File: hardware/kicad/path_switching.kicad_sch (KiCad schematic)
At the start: 25 parts, among them J601 VIN, Q601 CSD17577Q3A, Q602 CSD17577Q3A, Q603 CSD17577Q3A, Q604 CSD17577Q3A, U601 TC4427EOA, U602 MCP6561T-E/OT

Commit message: feat(hardware)!: draw draft A1 of the schematic around a Pico 2
A Raspberry Pi Pico 2 on two 1x20 sockets replaces the ESP32-S3
development board, the programmable logic device and the buffer
between the two boards (D-39 to D-43 of the specification). The former
interface and range logic sheets become two new ones:

- Controller: the Pico 2, the diodes that join its USB supply and the
  5 V rail of the carrier, resistor arrays in the SPI and acquisition
  lines, a reset button and a console header.
- Side Data: two shift registers that take the range, the status
  signals and the eight logic inputs with every sample.

The DUT connects through a 1x4 pin header and a lever terminal block
in parallel, both GND, VIN, VOUT, GND, and the logic port is a 1x10
header with VCC, GND, D7 to D0: the pin order of the PPK2 (D-44). A
solder jumper selects the supply of the DUT side of the level
translator. A transistor at the driver of the ampere switch holds it
open while VIN is above 5.5 V.

Reference designators are numbered as the annotation tool of KiCad
does by default (D-45). The numbering touches every sheet, so these
changes come in one commit. The symbol and the socket footprint of
the ESP32-S3 board leave the project library; the Pico 2 uses the
symbol and the footprint of the KiCad library.

The electrical rules check reports no errors and no warnings. The
parts stay candidates, and no program for the PIO blocks exists yet.

BREAKING CHANGE: the pins of the controller follow the new pin map of
section 5 of the specification.
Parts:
- removed J601: VIN, TerminalBlock_Phoenix:TerminalBlock_Phoenix_MKDS-1,5-2-5.08_1x02_P5.08mm_Horizontal, symbol Connector:Screw_Terminal_01x02
- added Q1: BSS138, Package_TO_SOT_SMD:SOT-23, symbol Transistor_FET:BSS138
- added R28: 1k, Resistor_SMD:R_0603_1608Metric, symbol Device:R
- R29: renamed from R606; value 1k -> 10k
- renumbered C601 to C41, C602 to C42, C603 to C43, C604 to C44, C605 to C45, D601 to D6, F601 to F2, Q601 to Q2, Q603 to Q3, Q602 to Q4, Q604 to Q5, R605 to R27, R607 to R30, R608 to R31, R609 to R32, R602 to R33, R601 to R34, R603 to R35, R604 to R36, TP602 to TP14, TP601 to TP15, U601 to U13, U602 to U14
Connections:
- net GATE_AMP: now also R28.1; no longer R29.1, U13.4 (IN_B)
- net GND: now also Q1.2 (S)
- net VIN_OV: now also Q1.1 (G)
- net VIN_RAW: now reaches F2.1
- new net: Q1.3 (D), R28.2, R29.1, U13.4 (IN_B)
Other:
- note added: "Mode switches: back-to-back pairs, gates at +12 V_A. Both off at reset; the controller breaks one before it makes the other. VIN: F2 and D6 take a reversed supply. VIN_OV goes high above 5.5 V and Q1 then holds the ampere switch open (it blocks up to 30 V), whatever the controller asks."
- note removed: "Mode switches: back-to-back pairs, gates at +12 V_A. Both off at reset; the logic device breaks one before it makes the other. VIN: F601 and D601 take a reversed supply. VIN_OV goes high above 5.5 V and the logic device then keeps the ampere switch open (blocks up to 30 V)."
- moved on the sheet: R27

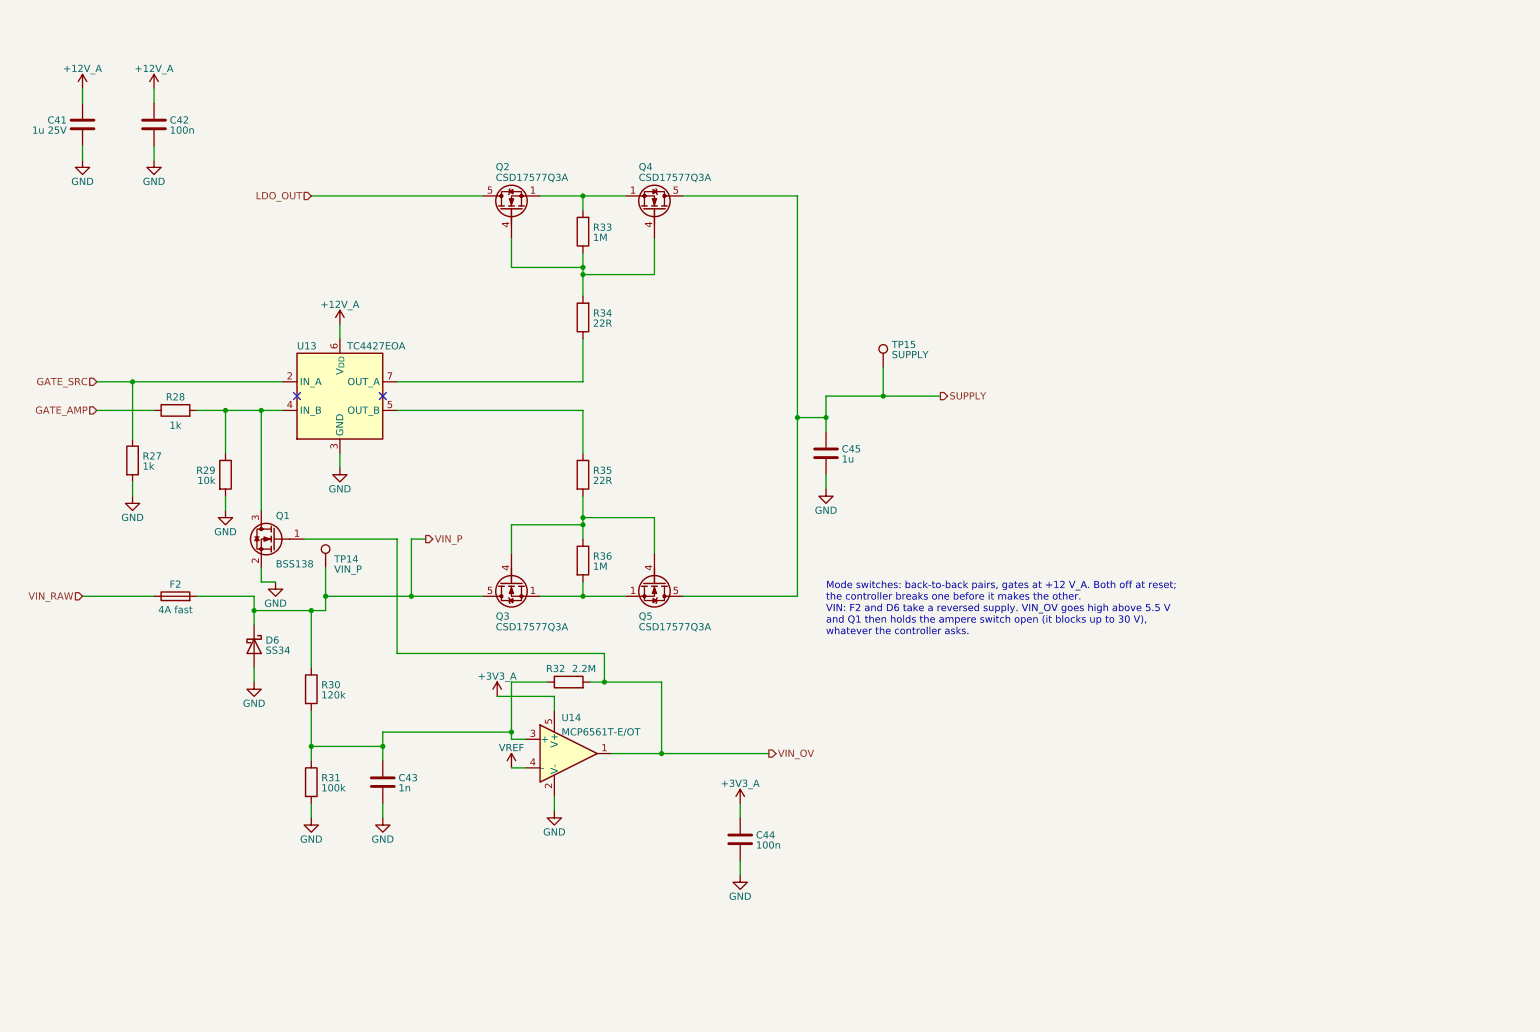
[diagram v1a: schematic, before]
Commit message: feat(hardware): draw draft A2 of the schematic
428 parts on 15 A4 pages, 14 sheets below the root sheet (D-83). Two
sheets are new: Logic Supplies, with the supervisor of the 5 V rail and
the two 3.3 V regulators, and Rail Monitor, with the comparators behind
PWR_GOOD.

The drawings follow the specification of draft A2: a current limiter
on each supply input and a priority multiplexer, a pre-regulator that
tracks the output of the linear regulator, a VIN path that withstands
-20 V to +20 V with its switch open, two diode-connected MOSFETs as
ladder clamp, thin-film and four-terminal shunts, ESD arrays at the CC
pins and at the VCC pin of the logic port. The reference designators
are numbered as KiCad numbers them (D-45), so they are not those of
draft A1.

The project library gains the symbol of the input multiplexer and two
footprints: the lever terminal block with pads of 1.9 mm x 2.3 mm and
the controller module without its antenna keep-out (D-85).

The electrical rules check reports no errors and no warnings. The
parts are candidates, and nothing is built or measured.
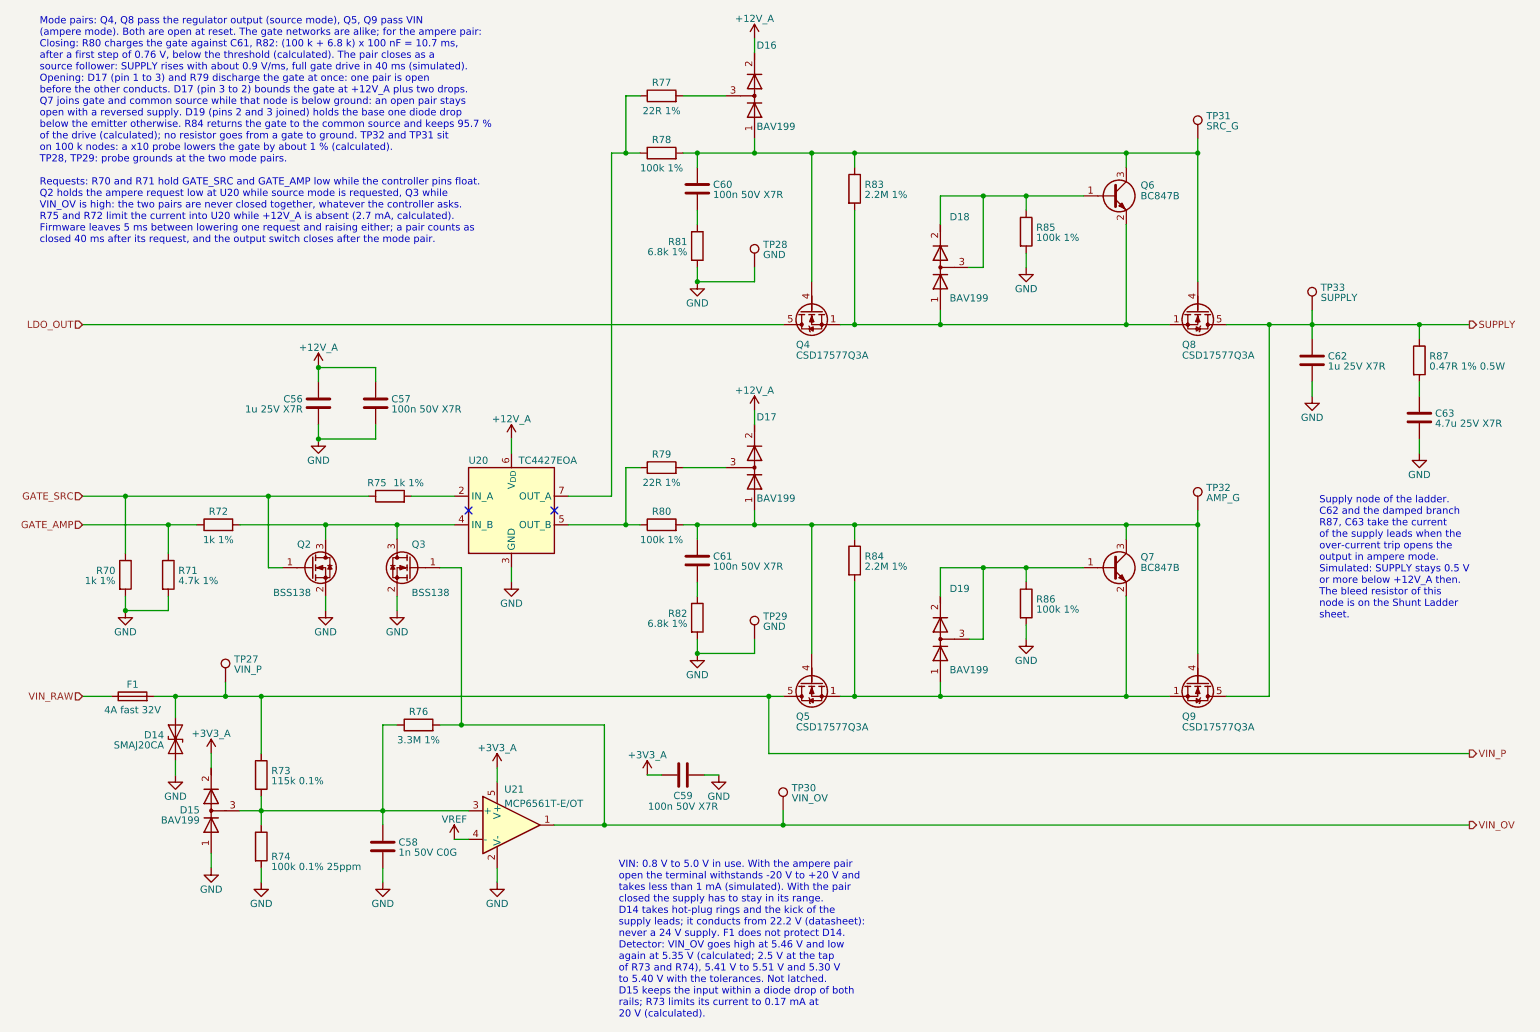
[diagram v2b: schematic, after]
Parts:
- added C60, C61: 100n 50V X7R, Capacitor_SMD:C_0603_1608Metric, symbol Device:C
- added C63: 4.7u 25V X7R, Capacitor_SMD:C_0805_2012Metric, symbol Device:C
- added D15, D16, D17, D18, D19: BAV199, Package_TO_SOT_SMD:SOT-23, symbol Device:D_Dual_Series_AKC
- added Q2: BSS138, Package_TO_SOT_SMD:SOT-23, symbol Transistor_FET:BSS138
- added Q6, Q7: BC847B, Package_TO_SOT_SMD:SOT-23, symbol Transistor_BJT:BC847
- added R75: 1k 1%, Resistor_SMD:R_0603_1608Metric, symbol Device:R
- added R78, R80, R85, R86: 100k 1%, Resistor_SMD:R_0603_1608Metric, symbol Device:R
- added R81, R82: 6.8k 1%, Resistor_SMD:R_0603_1608Metric, symbol Device:R
- added R87: 0.47R 1% 0.5W, Resistor_SMD:R_1206_3216Metric, symbol Device:R
- added TP28, TP29: GND, TestPoint:TestPoint_Pad_2.0x2.0mm, symbol Connector:TestPoint
- added TP30: VIN_OV, TestPoint:TestPoint_Pad_D1.5mm, symbol Connector:TestPoint
- added TP31: SRC_G, TestPoint:TestPoint_Pad_D1.5mm, symbol Connector:TestPoint
- added TP32: AMP_G, TestPoint:TestPoint_Pad_D1.5mm, symbol Connector:TestPoint
- C56: renamed from C41; value 1u 25V -> 1u 25V X7R; MPN (none) -> C0603C105K3RACTU; Manufacturer (none) -> KEMET
- C57: renamed from C42; value 100n -> 100n 50V X7R; MPN (none) -> C0603C104K5RACTU; Manufacturer (none) -> KEMET
- C58: renamed from C43; value 1n -> 1n 50V C0G; MPN (none) -> C0603C102J5GACTU; Manufacturer (none) -> KEMET
- C59: renamed from C44; value 100n -> 100n 50V X7R; MPN (none) -> C0603C104K5RACTU; Manufacturer (none) -> KEMET
- C62: renamed from C45; value 1u -> 1u 25V X7R; MPN (none) -> C0603C105K3RACTU; Manufacturer (none) -> KEMET
- D14: renamed from D6; value SS34 -> SMAJ20CA; symbol Device:D_Schottky -> Diode:SMAJ20CA; MPN (none) -> SMAJ20CA-E3/61; Manufacturer (none) -> Vishay
- F1: renamed from F2; value 4A fast -> 4A fast 32V; MPN (none) -> 0466004.NR; Manufacturer (none) -> Littelfuse
- Q3: renamed from Q1; MPN (none) -> BSS138-7-F; Manufacturer (none) -> Diodes Incorporated
- Q4: renamed from Q2; MPN (none) -> CSD17577Q3A; Manufacturer (none) -> Texas Instruments
- Q5: renamed from Q3; MPN (none) -> CSD17577Q3A; Manufacturer (none) -> Texas Instruments
- Q8: renamed from Q4; MPN (none) -> CSD17577Q3A; Manufacturer (none) -> Texas Instruments
- Q9: renamed from Q5; MPN (none) -> CSD17577Q3A; Manufacturer (none) -> Texas Instruments
- R70: renamed from R27; value 1k -> 1k 1%; MPN (none) -> CRCW06031K00FKEA; Manufacturer (none) -> Vishay
- R71: renamed from R29; value 10k -> 4.7k 1%; MPN (none) -> CRCW06034K70FKEA; Manufacturer (none) -> Vishay
- R72: renamed from R28; value 1k -> 1k 1%; MPN (none) -> CRCW06031K00FKEA; Manufacturer (none) -> Vishay
- R73: renamed from R30; value 120k -> 115k 0.1%; MPN (none) -> TNPW0603115KBEEA; Manufacturer (none) -> Vishay
- R74: renamed from R31; value 100k -> 100k 0.1% 25ppm; MPN (none) -> TNPW0603100KBEEA; Manufacturer (none) -> Vishay
- R76: renamed from R32; value 2.2M -> 3.3M 1%; MPN (none) -> CRCW06033M30FKEA; Manufacturer (none) -> Vishay
- R77: renamed from R34; value 22R -> 22R 1%; MPN (none) -> CRCW060322R0FKEA; Manufacturer (none) -> Vishay
- R79: renamed from R35; value 22R -> 22R 1%; MPN (none) -> CRCW060322R0FKEA; Manufacturer (none) -> Vishay
- R83: renamed from R33; value 1M -> 2.2M 1%; MPN (none) -> CRCW06032M20FKEA; Manufacturer (none) -> Vishay
- R84: renamed from R36; value 1M -> 2.2M 1%; MPN (none) -> CRCW06032M20FKEA; Manufacturer (none) -> Vishay
- TP27: renamed from TP14; now left out of the parts list
- TP33: renamed from TP15; now left out of the parts list
- U20: renamed from U13; MPN (none) -> TC4427EOA713; Manufacturer (none) -> Microchip
- U21: renamed from U14; MPN (none) -> MCP6561T-E/OT; Manufacturer (none) -> Microchip
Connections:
- net +12V_A: now also D16.2 (K), D17.2 (K)
- net +3V3_A: now also D15.2 (K)
- net GATE_AMP: now also R71.1
- net GATE_SRC: now also Q2.1 (G), R75.1; no longer U20.2 (IN_A)
- net GND: now also C63.2, D15.1 (A), Q2.2 (S), R81.2, R82.2, R85.2, R86.2, TP28.1, TP29.1
- net SUPPLY: now also R87.1
- net VIN_OV: now also TP30.1
- net at C58.1, R73.2, R74.1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: now also D15.3 (common)
- net at Q4.1 (S), Q4.2 (S), Q4.3 (S)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: now also D18.1 (A), Q6.2 (E)
- net at Q4.4 (G), Q8.4 (G), R83.1: now also C60.1, D16.1 (A), Q6.3 (C), R78.2, TP31.1; no longer R77.2
- net at Q3.3 (D), R72.2, U20.4 (IN_B): now also Q2.3 (D); no longer R71.1
- net at R79.1, U20.5 (OUT_B): now also R80.1
- net at Q5.4 (G), Q9.4 (G), R84.1: now also C61.1, D17.1 (A), Q7.3 (C), R80.2, TP32.1; no longer R79.2
- net at Q5.1 (S), Q5.2 (S), Q5.3 (S)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: now also D19.1 (A), Q7.2 (E)
- net at R77.1, U20.7 (OUT_A): now also R78.1
- new net: C60.2, R81.1
- new net: D18.2 (K), D18.3 (common), Q6.1 (B), R85.1
- new net: C61.2, R82.1
- new net: R75.2, U20.2 (IN_A)
- new net: D17.3 (common), R79.2
- new net: D16.3 (common), R77.2
- new net: D19.2 (K), D19.3 (common), Q7.1 (B), R86.1
- new net: C63.1, R87.2
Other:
- note added: "Mode pairs: Q4, Q8 pass the regulator output (source mode), Q5, Q9 pass VIN (ampere mode). Both are open at reset. The gate networks are alike; for the ampere pair: Closing: R80 charges the gate against C61, R82: (100 k + 6.8 k) x 100 nF = 10.7 ms, after a first step of 0.76 V, below the threshold (calculated). The pair closes as a source follower: SUPPLY rises with about 0.9 V/ms, full gate driv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"
- note added: "Supply node of the ladder. C62 and the damped branch R87, C63 take the current of the supply leads when the over-current trip opens the output in ampere mode. Simulated: SUPPLY stays 0.5 V or more below +12V_A then. The bleed resistor of this node is on the Shunt Ladder sheet."
- note added: "VIN: 0.8 V to 5.0 V in use. With the ampere pair open the terminal withstands -20 V to +20 V and takes less than 1 mA (simulated). With the pair closed the supply has to stay in its range. D14 takes hot-plug rings and the kick of the supply leads; it conducts from 22.2 V (datasheet): never a 24 V supply. F1 does not protect D14. Detector: VIN_OV goes high at 5.46 V and low again at 5.35 V (calcul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"
- note removed: "Mode switches: back-to-back pairs, gates at +12 V_A. Both off at reset; the controller breaks one before it makes the other. VIN: F2 and D6 take a reversed supply. VIN_OV goes high above 5.5 V and Q1 then holds the ampere switch open (it blocks up to 30 V), whatever the controller asks."
- moved on the sheet: C56, C57, C58, C59, C62, F1, Q3, Q4, Q5, Q8, Q9, R70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
